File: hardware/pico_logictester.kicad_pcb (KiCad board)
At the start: 2 copper layers, 92.8 x 67.6 mm, 29 parts, among them J1 LOGIC_INPUT, J2 GPIO_5_28, J3 AKKU, J4 STEP_UP_IN, J5 5V VERSORGUNG, J6 TFT Display, Q1 AO3401A, Q2 BC547, SW1 SW_Push, U1 74HC245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

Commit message: Update pico_logictester.kicad_pcb
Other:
- board text added: "Achtung! Routing noch nicht komplett!"
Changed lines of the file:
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@@
 		(layer "Edge.Cuts")
+	)
+	(gr_text "Achtung! Routing noch nicht komplett!"
+		(at 59.8424 68.5038 0)
+		(layer "Edge.Cuts")
+		(effects
+			(font
+				(size 1 1)
+				(thickness 0.15)
+			)
+			(justify left bottom)
+		)
 	)
 	(segment

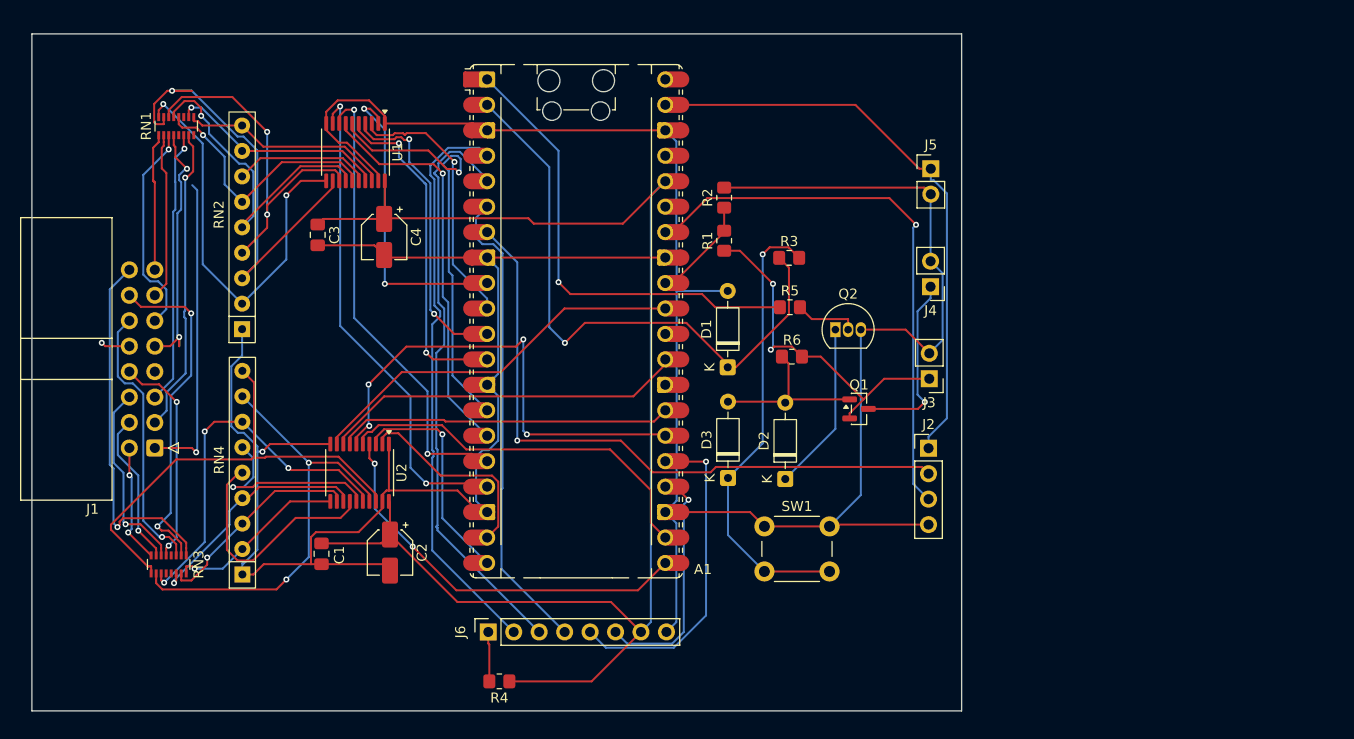
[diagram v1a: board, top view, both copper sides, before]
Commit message: hardware: new pcb layout
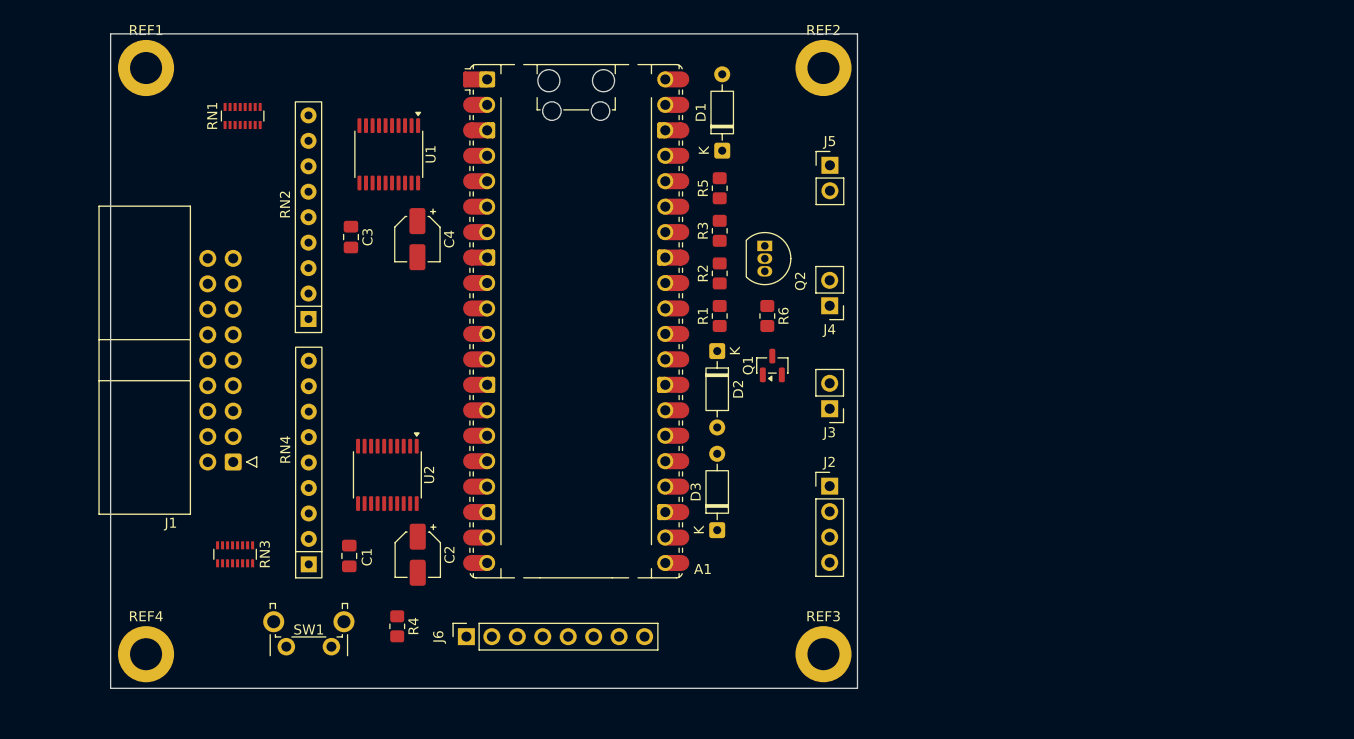
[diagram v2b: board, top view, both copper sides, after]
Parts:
- added REF1: MountingHole_3.2mm_M3_DIN965_Pad, MountingHole:MountingHole_3.2mm_M3_DIN965_Pad, F.Cu at (70.5, 69.8)
- added REF2: MountingHole_3.2mm_M3_DIN965_Pad, MountingHole:MountingHole_3.2mm_M3_DIN965_Pad, F.Cu at (138.1, 69.7)
- added REF3: MountingHole_3.2mm_M3_DIN965_Pad, MountingHole:MountingHole_3.2mm_M3_DIN965_Pad, F.Cu at (138.1, 128.2)
- added REF4: MountingHole_3.2mm_M3_DIN965_Pad, MountingHole:MountingHole_3.2mm_M3_DIN965_Pad, F.Cu at (70.5, 128.2)
- J1: footprint Connector_IDC:IDC-Header_2x08_P2.54mm_Horizontal -> Connector_IDC:IDC-Header_2x09_P2.54mm_Horizontal
- SW1: footprint Button_Switch_THT:SW_PUSH_6mm_H5mm -> Button_Switch_THT:SW_Tactile_SPST_Angled_PTS645Vx83-2LFS
- moved SW1 44.8 mm to (89.0, 127.5), turned to 180 degrees
- moved D1 21.6 mm to (128.0, 78.0)
- moved D2 14.5 mm to (127.5, 98.0), turned to -90 degrees
- moved R5 13.8 mm to (127.8, 81.8), turned to 90 degrees
- moved R4 11.6 mm to (95.6, 125.5), turned to -90 degrees
- moved Q2 10.9 mm to (132.2, 87.5), turned to -90 degrees
- moved J2 10.6 mm to (138.7, 111.5)
- moved J3 10.4 mm to (138.7, 103.8)
- moved J4 10.2 mm to (138.7, 93.5)
- moved J5 10.1 mm to (138.8, 79.5)
- moved Q1 9.68 mm to (133.0, 99.4), turned to 90 degrees
- moved J1 7.95 mm to (79.2, 109.1)
- moved R2 7.58 mm to (127.8, 90.2)
- moved R1 7.52 mm to (127.8, 94.5)
- moved R3 7.44 mm to (127.8, 86.0), turned to 90 degrees
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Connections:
- A1 pad 33: GND -> AGND
- R2 pad 2: GND -> AGND
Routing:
- net GND: track 343.7 -> 0.00 mm, vias 1 -> 0
- net +3.3V: track 142.2 -> 0.00 mm
- net GPIO_5: track 65.7 -> 0.00 mm, vias 1 -> 0
- net SENSE_GPIO: track 61.2 -> 0.00 mm, vias 1 -> 0
- net TFT_DC: track 59.9 -> 0.00 mm
- net +5V: track 58.6 -> 0.00 mm
- net TFT_CS: track 58.3 -> 0.00 mm
- net GPIO_28: track 55.7 -> 0.00 mm, vias 1 -> 0
- net Net-(RN1-R2.2): track 51.6 -> 0.00 mm, vias 1 -> 0
- net LOGIC_7: track 49.4 -> 0.00 mm, vias 2 -> 0
- net LOGIC_12: track 48.2 -> 0.00 mm, vias 4 -> 0
- net TFT_RST: track 48.1 -> 0.00 mm
- net Net-(RN3-R8.2): track 47.4 -> 0.00 mm
- net SYSTEM_POWER_PIN: track 47.1 -> 0.00 mm, vias 1 -> 0
- net LOGIC_6: track 46.1 -> 0.00 mm, vias 2 -> 0
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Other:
- board size 92.8 x 67.6 mm -> 74.5 x 65.3 mm

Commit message: remove files
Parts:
- removed REF1, REF2, REF3, REF4: MountingHole_3.2mm_M3_DIN965_Pad, MountingHole:MountingHole_3.2mm_M3_DIN965_Pad
- J1: footprint Connector_IDC:IDC-Header_2x09_P2.54mm_Horizontal -> Connector_IDC:IDC-Header_2x08_P2.54mm_Horizontal
- SW1: footprint Button_Switch_THT:SW_Tactile_SPST_Angled_PTS645Vx83-2LFS -> Button_Switch_THT:SW_PUSH_6mm_H9.5mm
- moved J1 48.1 mm to (127.3, 110.8)
- moved SW1 47.7 mm to (136.5, 131.6)
- moved C1 47.6 mm to (138.3, 121.3)
- moved R4 47.6 mm to (143.1, 128.3)
- moved RN2 47.6 mm to (134.2, 97.7)
- moved U1 47.6 mm to (142.2, 81.2)
- moved U2 47.6 mm to (142.1, 113.2)
- moved A1 47.6 mm to (160.9, 97.9)
- moved C2 47.6 mm to (145.1, 121.2)
- moved C4 47.6 mm to (145.1, 89.7)
- moved RN1 47.6 mm to (127.6, 77.4)
- moved RN3 47.6 mm to (126.9, 121.1)
- moved RN4 47.6 mm to (134.2, 122.1)
- moved C3 47.6 mm to (138.5, 89.5)
- moved D1 47.6 mm to (175.5, 80.9)
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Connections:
- A1 pad 33: AGND -> GND
- R2 pad 2: AGND -> GND
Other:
- board text removed: "Achtung! Routing noch nicht komplett!"

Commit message: hardware: bauckup
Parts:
- added G***: LOGO, logos_tk:logo_01_10_7mm_fsilk, F.Cu at (142.8, 99.5)
- added REF**: KiCad-Logo2_12mm_SilkScreen, Symbol:KiCad-Logo2_12mm_SilkScreen, B.Cu at (159.5, 100.2)
- added REF1: MountingHole_3.2mm_M3_DIN965_Pad, MountingHole:MountingHole_3.2mm_M3_DIN965_Pad, F.Cu at (118.2, 75.8)
- added REF2: MountingHole_3.2mm_M3_DIN965_Pad, MountingHole:MountingHole_3.2mm_M3_DIN965_Pad, F.Cu at (185.5, 75.8)
- added REF3: MountingHole_3.2mm_M3_DIN965_Pad, MountingHole:MountingHole_3.2mm_M3_DIN965_Pad, F.Cu at (185.5, 131.0)
- added REF4: MountingHole_3.2mm_M3_DIN965_Pad, MountingHole:MountingHole_3.2mm_M3_DIN965_Pad, F.Cu at (118.0, 131.0)
- J1: value LOGIC_INPUT -> Conn_02x09_Odd_Even; footprint Connector_IDC:IDC-Header_2x08_P2.54mm_Horizontal -> Connector_IDC:IDC-Header_2x09_P2.54mm_Horizontal
- SW1: footprint Button_Switch_THT:SW_PUSH_6mm_H9.5mm -> Button_Switch_THT:SW_Tactile_SPST_Angled_PTS645Vx83-2LFS
- moved SW1 0.62 mm to (136.5, 131.0)
- moved J1 0.61 mm to (127.0, 111.3)
- moved J3 0.17 mm to (186.2, 106.8)
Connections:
- A1 pad 33: GND -> AGND
- R2 pad 2: GND -> AGND
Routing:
- net GND: track 0.00 -> 342.5 mm
- net +3.3V: track 0.00 -> 134.2 mm
- net Net-(D3-K): track 0.00 -> 88.1 mm, vias 0 -> 1
- net LOGIC_15: track 0.00 -> 82.5 mm, vias 0 -> 1
- net TFT_DC: track 0.00 -> 79.4 mm
- net TFT_CS: track 0.00 -> 71.9 mm, vias 0 -> 2
- net LOGIC_7: track 0.00 -> 61.8 mm, vias 0 -> 2
- net LOGIC_10: track 0.00 -> 54.1 mm, vias 0 -> 2
- net +5V: track 0.00 -> 52.1 mm
- net GPIO_5: track 0.00 -> 50.3 mm
- net SYSTEM_POWER_PIN: track 0.00 -> 48.2 mm, vias 0 -> 1
- net Net-(RN3-R8.2): track 0.00 -> 46.8 mm, vias 0 -> 2
- net TFT_RST: track 0.00 -> 46.1 mm
- net GPIO_28: track 0.00 -> 45.7 mm
- net LOGIC_11: track 0.00 -> 41.7 mm
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- added copper zone on B.Cu, net GND
- added copper zone on F.Cu, net GND
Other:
- board size 74.5 x 65.3 mm -> 74.5 x 62.3 mm
- board text added: "+"
- board text added: "+5V"
- board text added: "0"
- board text added: "1"
- board text added: "10"
- board text added: "11"
- board text added: "12"
- board text added: "13"
- board text added: "14"
- board text added: "15"
- board text added: "2"
- board text added: "3"
- board text added: "3.3V"
- board text added: "4"
- board text added: "5"
- board text added: "6"
- board text added: "7"
- board text added: "8"
- board text added: "9"
- board text added: "AKKU+"
- board text added: "AKKU-"
- board text added: "CS"
- board text added: "DC"
- board text added: "DCLK"
- board text added: "DI"
- board text added: "GND"
- board text added: "GPIO_28"
- board text added: "GPIO_5"
- board text added: "LED"
- board text added: "Pico Logictester SCH:1.0 / PCB:1.0"
- board text added: "RS"
- board text added: "STEP_UP_IN"
- board text added: "STEP_UP_OUT"
- board text added: "TFT Display"
- board text added: "[01.2026]"
- board text added: "by th.kattanek and community"

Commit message: hardware: pcb_1.0 fertig gestellt und Gerberfiles erstellt.
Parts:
- moved D1 0.45 mm to (175.5, 81.3)
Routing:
- net LOGIC_15: track 82.5 -> 37.1 mm, vias 1 -> 0
- net TFT_RST: track 46.1 -> 76.4 mm, vias 0 -> 1
- net TFT_DC: track 79.4 -> 50.5 mm
- net GND: track 342.5 -> 318.0 mm
- net Net-(D3-K): track 88.1 -> 107.7 mm
- net SYSTEM_POWER_PIN: track 48.2 -> 29.2 mm, vias 1 -> 0
- net LOGIC_1: track 22.5 -> 39.7 mm
- net Net-(J1-Pin_7): track 26.3 -> 43.4 mm
- net LOGIC_7: track 61.8 -> 44.8 mm, vias 2 -> 3
- net Net-(RN1-R1.2): track 36.0 -> 52.1 mm, vias 2 -> 1
- net Net-(RN1-R6.2): track 36.7 -> 21.9 mm
- net LOGIC_12: track 32.0 -> 46.7 mm, vias 0 -> 3
- net LOGIC_10: track 54.1 -> 40.6 mm
- net LOGIC_5: track 36.6 -> 50.0 mm
- net Net-(RN1-R7.2): track 30.2 -> 18.5 mm, vias 4 -> 0
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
